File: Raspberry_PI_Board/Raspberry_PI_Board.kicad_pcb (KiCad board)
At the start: 2 copper layers, 56 x 80 mm, 6 parts, among them J1 Conn_02x08_Odd_Even, J2 Conn_02x08_Odd_Even, U3 RASPBERRY_PI_ZERO_2_W

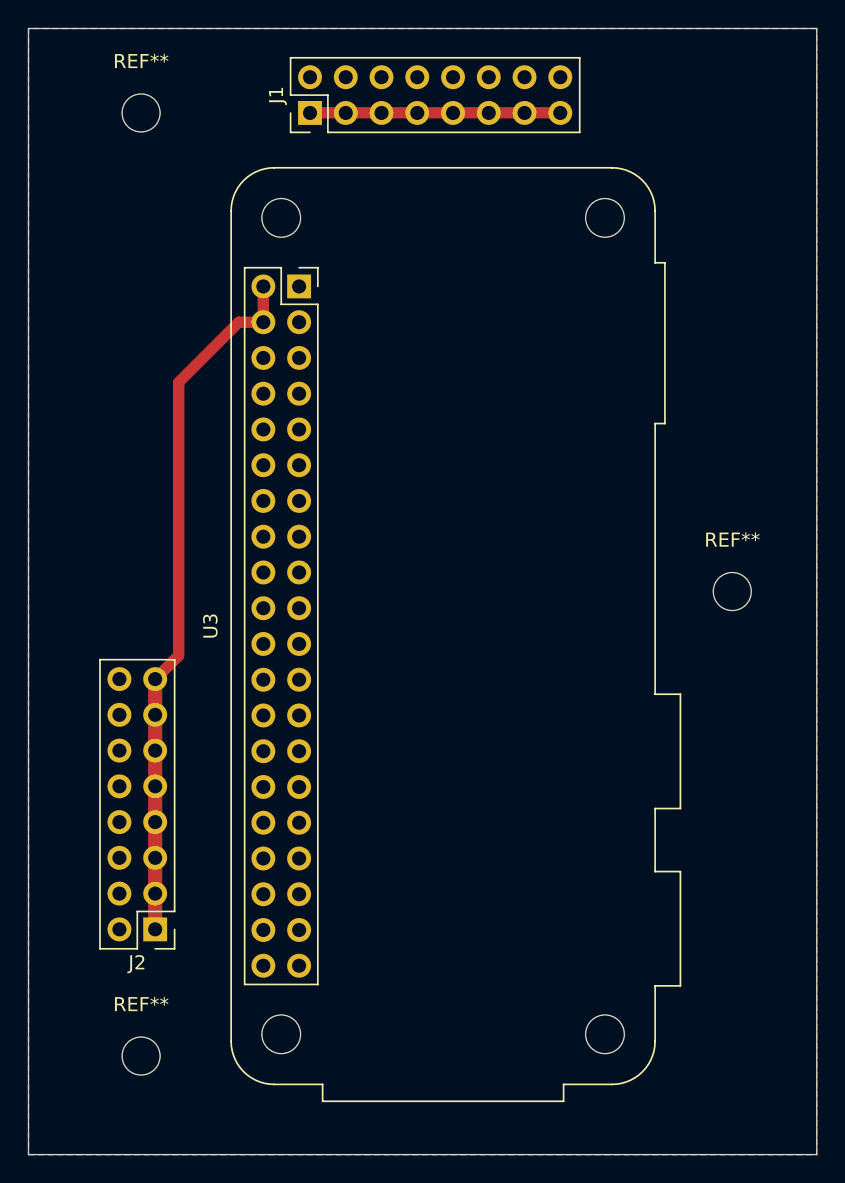
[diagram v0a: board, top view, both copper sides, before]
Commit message: Fix flipped components
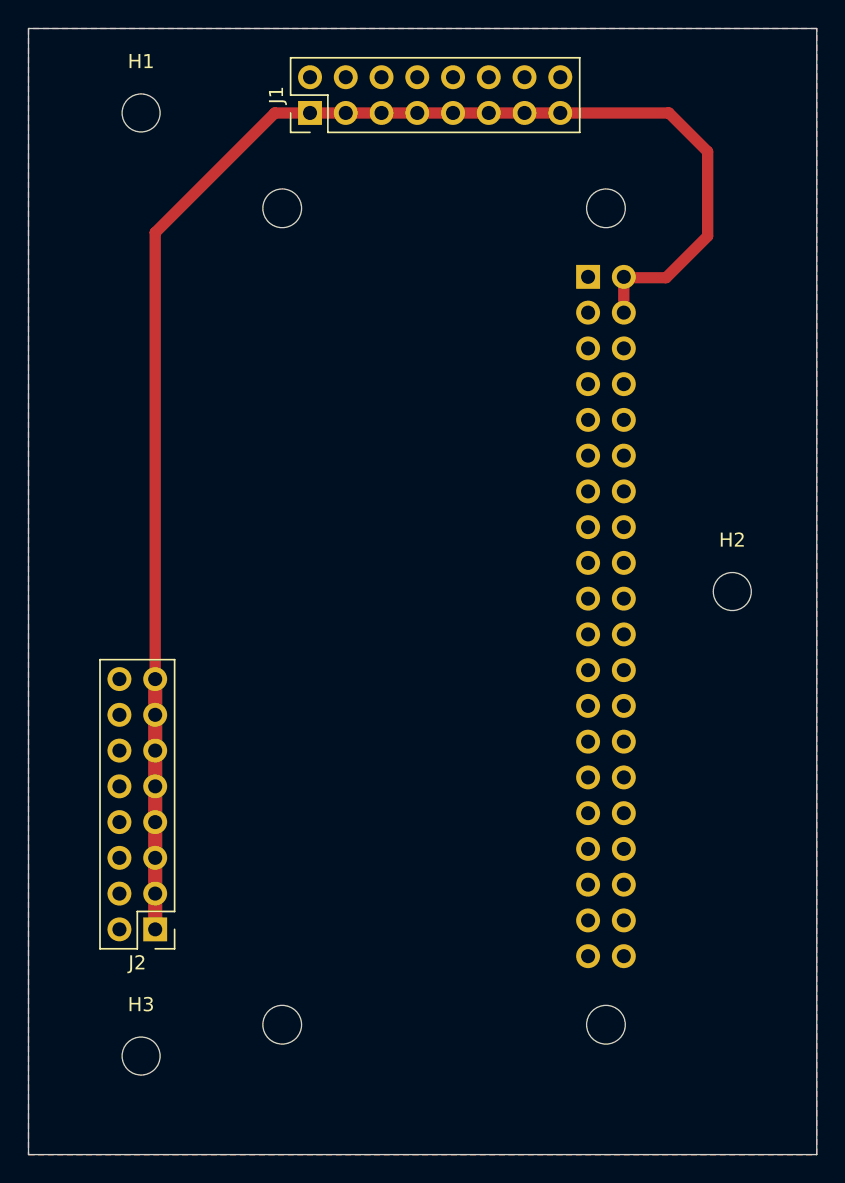
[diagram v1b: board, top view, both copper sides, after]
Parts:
- U3: moved to B.Cu
- moved U3 20.5 mm to (69.8, 47.6), turned to 180 degrees
- renumbered REF** to H1, REF** to H2, REF** to H3
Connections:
- J1 pad 1: /Passthrough_Voltage -> /+5V
- J1 pad 11: /Passthrough_Voltage -> /+5V
- J1 pad 13: /Passthrough_Voltage -> /+5V
- J1 pad 15: /Passthrough_Voltage -> /+5V
- J1 pad 3: /Passthrough_Voltage -> /+5V
- J1 pad 5: /Passthrough_Voltage -> /+5V
- J1 pad 7: /Passthrough_Voltage -> /+5V
- J1 pad 9: /Passthrough_Voltage -> /+5V
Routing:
- net /+5V: track 49.9 -> 109.2 mm
- net /Passthrough_Voltage: track 17.8 -> 0.00 mm
